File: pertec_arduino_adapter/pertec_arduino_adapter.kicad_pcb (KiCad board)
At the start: 2 copper layers, 88.9 x 53.3 mm, 15 parts, among them J1 Pertec J1, J10 SPI flash connector, J2 Pertec J2, J3 Mates with POWER, J4 Mates with ANALOG IN A0-A7, J5 Mates with ANALOG IN A8-A15, J6 Mates with JP6 ANALOG IN A8-A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, J7 Mates with PWM 0-7, J8 Mates with COMMUNICATION 14-21, J9 Mates with XIO DIGITAL 22-53

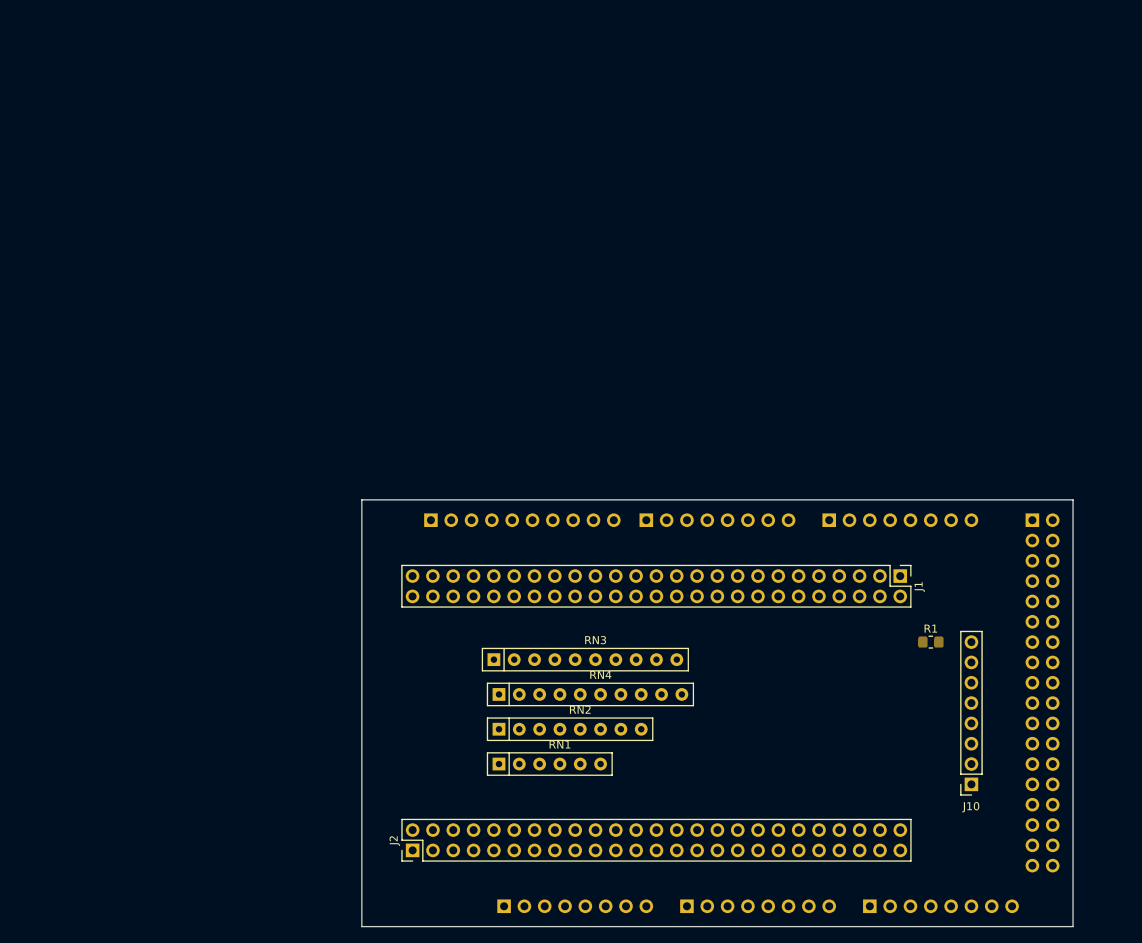
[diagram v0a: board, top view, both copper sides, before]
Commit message: Development checkpoint: started work on design for Adafruit Metro M4 Grand Central.  I'm aborting that development path and switching to the Teensy 4.1 because it's far faster and actually available.
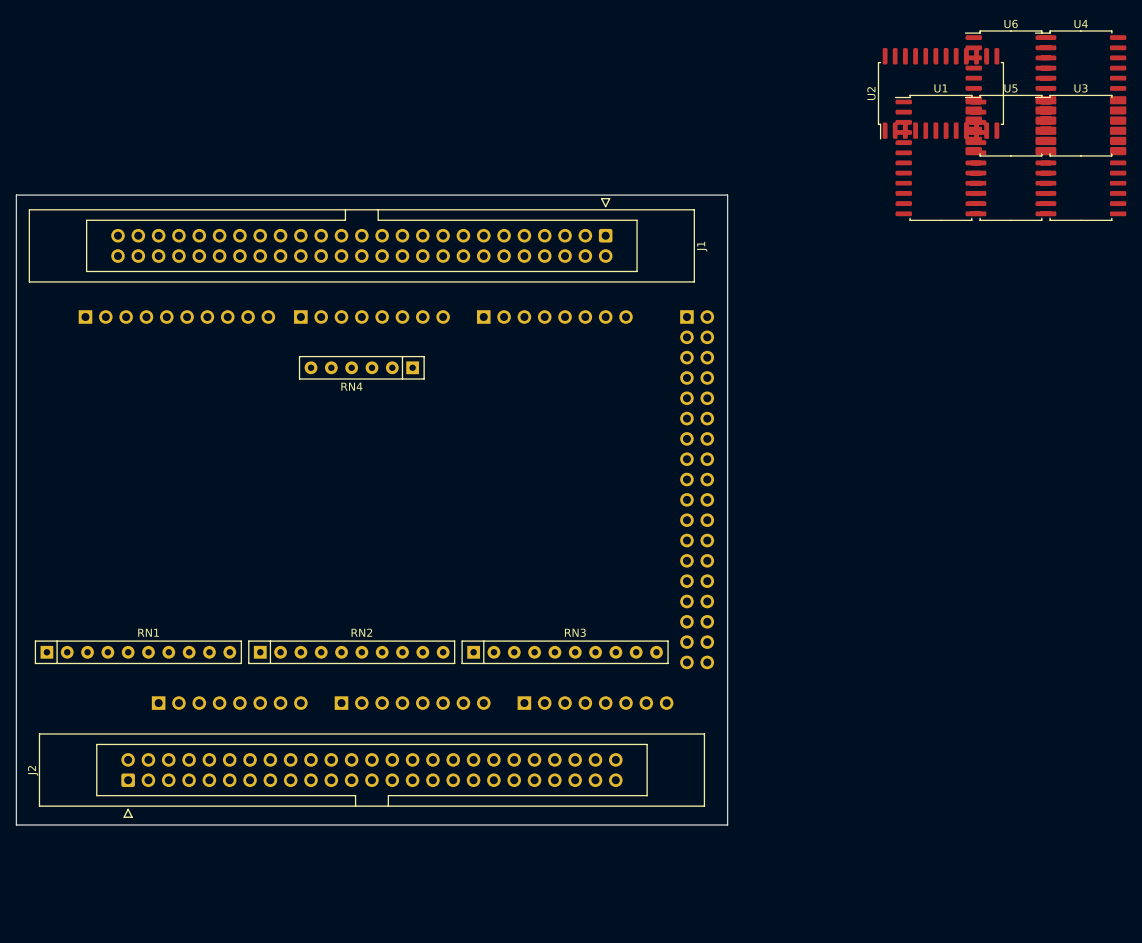
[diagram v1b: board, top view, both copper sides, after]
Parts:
- removed J10: SPI flash connector, Connector_PinSocket_2.54mm:PinSocket_1x08_P2.54mm_Vertical
- removed R1: 10 kΩ, Resistor_SMD:R_0805_2012Metric_Pad1.20x1.40mm_HandSolder
- added U1: SN74AVC8T245PW, pertec_arduino_adapter:SOIC-24W_7.5x15.4mm_P1.27mm, F.Cu at (191.8, 30.9)
- added U2: SN74AVC8T245PW, pertec_arduino_adapter:SOIC-24W_7.5x15.4mm_P1.27mm, F.Cu at (191.8, 22.9)
- added U3: SN74AVC8T245PW, pertec_arduino_adapter:SOIC-24W_7.5x15.4mm_P1.27mm, F.Cu at (209.3, 30.9)
- added U4: SN74AVC8T245PW, pertec_arduino_adapter:SOIC-24W_7.5x15.4mm_P1.27mm, F.Cu at (209.3, 22.9)
- added U5: SN74AVC8T245PW, pertec_arduino_adapter:SOIC-24W_7.5x15.4mm_P1.27mm, F.Cu at (200.5, 30.9)
- added U6: SN74AVC8T245PW, pertec_arduino_adapter:SOIC-24W_7.5x15.4mm_P1.27mm, F.Cu at (200.5, 22.9)
- J1: value Pertec J1 -> Conn_02x25_Odd_Even; footprint Connector_PinHeader_2.54mm:PinHeader_2x25_P2.54mm_Vertical -> pertec_arduino_adapter:IDC-Header_2x25_P2.54mm_Latch_Vertical
- J2: value Pertec J2 -> Conn_02x25_Odd_Even; footprint Connector_PinHeader_2.54mm:PinHeader_2x25_P2.54mm_Vertical -> pertec_arduino_adapter:IDC-Header_2x25_P2.54mm_Latch_Vertical
- J3: value Mates with POWER -> POWER; footprint Connector_PinHeader_2.54mm:PinHeader_1x08_P2.54mm_Vertical -> pertec_arduino_adapter:PinHeader_1x08_P2.54mm_Vertical
- J4: value Mates with ANALOG IN A0-A7 -> ANALOGL; footprint Connector_PinHeader_2.54mm:PinHeader_1x08_P2.54mm_Vertical -> pertec_arduino_adapter:PinHeader_1x08_P2.54mm_Vertical
- J5: value Mates with ANALOG IN A8-A15 -> ANALOGH; footprint Connector_PinHeader_2.54mm:PinHeader_1x08_P2.54mm_Vertical -> pertec_arduino_adapter:PinHeader_1x08_P2.54mm_Vertical
- J6: value Mates with JP6 ANALOG IN A8-A13+others -> Conn_02x18_Odd_Even; footprint Connector_PinHeader_2.54mm:PinHeader_1x10_P2.54mm_Vertical -> pertec_arduino_adapter:PinHeader_2x18_P2.54mm_Vertical_Mirror
- J7: value Mates with PWM 0-7 -> IOH; footprint Connector_PinHeader_2.54mm:PinHeader_1x08_P2.54mm_Vertical -> pertec_arduino_adapter:PinHeader_1x10_P2.54mm_Vertical
- J8: value Mates with COMMUNICATION 14-21 -> IOL; footprint Connector_PinHeader_2.54mm:PinHeader_1x08_P2.54mm_Vertical -> pertec_arduino_adapter:PinHeader_1x08_P2.54mm_Vertical
- J9: value Mates with XIO DIGITAL 22-53 -> UART; footprint pertec_arduino_adapter:PinHeader_2x18_P2.54mm_Vertical_Mirror -> pertec_arduino_adapter:PinHeader_1x08_P2.54mm_Vertical
- RN1: value R_Divider_Network04_Split -> R1=220Ω, R2=330Ω; footprint Resistor_THT:R_Array_SIP6 -> pertec_arduino_adapter:R_Array_SIP10
- RN2: value R_Divider_Network06_Split -> R1=220Ω, R2=330Ω; footprint Resistor_THT:R_Array_SIP8 -> pertec_arduino_adapter:R_Array_SIP10
- RN3: value R_Divider_Network08_Split -> R1=220Ω, R2=330Ω; footprint Resistor_THT:R_Array_SIP10 -> pertec_arduino_adapter:R_Array_SIP10
- RN4: value R_Divider_Network08_Split -> R1=220Ω, R2=330Ω; footprint Resistor_THT:R_Array_SIP10 -> pertec_arduino_adapter:R_Array_SIP6
- moved J7 74.6 mm to (84.8, 50.8)
- moved J9 73.1 mm to (134.6, 50.8), turned to -90 degrees
- moved J8 70.8 mm to (111.8, 50.8)
- moved RN1 58.2 mm to (80.0, 92.7)
- moved J1 56.3 mm to (149.9, 40.6)
- moved J4 50.1 mm to (116.8, 99.1)
- moved J5 50.1 mm to (139.7, 99.1)
- moved J3 50.1 mm to (94.0, 99.1)
- moved RN4 42.2 mm to (125.7, 57.1), turned to 180 degrees
- moved J6 40.9 mm to (160.0, 50.8), turned to 180 degrees
- moved J2 36.6 mm to (90.2, 108.7)
- moved RN2 31.4 mm to (106.7, 92.7)
- moved RN3 2.70 mm to (133.4, 92.7)
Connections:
- J1 pad 13: (no net) -> GNDREF
- J1 pad 15: (no net) -> GNDREF
- J1 pad 35: (no net) -> GNDREF
- J1 pad 43: (no net) -> GNDREF
- J2 pad 46: ITDA1 -> ITAD1
- J2 pad 49: (no net) -> GNDREF
- J2 pad 50: IDEN -> IHISP
- J3 pad 1: (no net) -> unconnected-(J3-Pad1)
- J3 pad 2: +5V -> +3V3
- J3 pad 3: (no net) -> ~{RESET}
- J3 pad 4: (no net) -> +3V3
- J3 pad 8: (no net) -> /VIN
- J4 pad 1: IR7 -> A0
- J4 pad 2: IR6 -> A1
- J4 pad 3: IR5 -> A2
- J4 pad 4: IR4 -> A3
- J4 pad 5: IR3 -> A4
- J4 pad 6: IR2 -> A5
- J4 pad 7: IR1 -> A6
- J4 pad 8: IR0 -> A7
- J5 pad 1: IFBY -> A8
- J5 pad 2: ILDP -> A9
- J5 pad 3: IEOT -> A10
- J5 pad 4: IRDY -> A11
- J5 pad 5: IRWD -> A12
- J5 pad 6: IFPT -> A13
- J5 pad 7: ISPEED -> A14
- J5 pad 8: IONL -> A15
- J6 pad 1: IHER -> +5V
- J6 pad 10: (no net) -> PCC_XCLK
- J6 pad 2: IFMK -> +5V
- J6 pad 3: (no net) -> D22
- J6 pad 4: GNDREF -> A10
- J6 pad 5: IRTH1 -> SCL_1
- J6 pad 6: IRTH2 -> SDA_1
- J6 pad 7: ILOL -> PCC_DEN1
- J6 pad 8: ISGL -> PCC_DEN2
- J6 pad 9: (no net) -> PCC_CLK
- J7 pad 1: (no net) -> SCL
- J7 pad 2: (no net) -> SDA
- J7 pad 3: (no net) -> AREF
- J7 pad 4: (no net) -> GND
- J7 pad 5: IRSTR -> D13
- J7 pad 6: IWSTR -> D12
- J7 pad 7: (no net) -> D11
- J7 pad 8: (no net) -> D10
- J8 pad 1: (no net) -> D7
- J8 pad 2: (no net) -> D6
- J8 pad 3: (no net) -> D5
- J8 pad 4: (no net) -> D4
- J8 pad 5: IDBY -> D3
- J8 pad 6: ICER -> D2
- J8 pad 7: IFMK -> D1
- J8 pad 8: IHER -> D0
- J9 pad 1: +5V -> UART3_TX
- J9 pad 2: +5V -> UART3_RX
- J9 pad 3: IW7 -> UART2_TX
- J9 pad 4: IW6 -> UART2_RX
- J9 pad 5: IW5 -> UART1_TX
- J9 pad 6: IW4 -> UART1_RX
- J9 pad 7: IW3 -> SDA
- J9 pad 8: IW2 -> SCL
- RN1 pad 2: IR3 -> IRP
- RN1 pad 3: ISPEED -> IR0
- RN1 pad 4: ICER -> IR1
- RN1 pad 5: IONL -> ILDP
- RN1 pad 6: +5V -> IR4
- RN2 pad 2: IRWD -> IFMK
- RN2 pad 3: IRP -> IDENT
- RN2 pad 4: IRSTR -> IR5
- RN2 pad 5: IWSTR -> IEOT
- RN2 pad 6: IDBY -> INRZ
- RN2 pad 7: IR2 -> IRDY
- RN2 pad 8: +5V -> IRWD
- RN3 pad 2: ILDP -> IRSTR
- RN3 pad 3: IHER -> IWSTR
- RN3 pad 4: INRZ -> IDBY
- RN3 pad 5: IFMK -> ISPEED
- RN3 pad 6: IR0 -> ICER
- RN3 pad 7: IR6 -> IONL
- RN3 pad 8: IFPT -> unconnected-(RN3-Pad8)
- RN3 pad 9: IR7 -> unconnected-(RN3-Pad9)
- RN4 pad 2: IR4 -> IFBY
- RN4 pad 3: IRDY -> IR2
- RN4 pad 4: IDENT -> IR3
- RN4 pad 5: IR1 -> unconnected-(RN4-Pad5)
- RN4 pad 6: IR5 -> +5V
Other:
- board size 88.9 x 53.3 mm -> 88.9 x 78.7 mm
- net class Default removed

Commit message: Development checkpoint: schematic complete, passes ERC, started layout.
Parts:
- removed J9: UART, pertec_arduino_adapter:PinHeader_1x08_P2.54mm_Vertical
- added BT1: CR2032, pertec_arduino_adapter:BatteryHolder_Keystone_1058_1x2032, F.Cu at (158.8, 74.9)
- added C1: 0.1 μF, pertec_arduino_adapter:C_Rect_L4.0mm_W2.5mm_P2.50mm, F.Cu at (114.3, 80.0)
- added C10: 0.1 μF, pertec_arduino_adapter:C_0805_2012Metric_Pad1.18x1.45mm_HandSolder, B.Cu at (97.8, 114.3)
- added C11: 0.1 μF, pertec_arduino_adapter:C_0805_2012Metric_Pad1.18x1.45mm_HandSolder, B.Cu at (157.7, 96.5)
- added C12: 0.1 μF, pertec_arduino_adapter:C_0805_2012Metric_Pad1.18x1.45mm_HandSolder, B.Cu at (171.4, 81.3)
- added C13: 0.1 μF, pertec_arduino_adapter:C_0805_2012Metric_Pad1.18x1.45mm_HandSolder, B.Cu at (172.7, 92.7)
- added C14: 0.1 μF, pertec_arduino_adapter:C_0805_2012Metric_Pad1.18x1.45mm_HandSolder, B.Cu at (166.4, 64.8)
- added C2: 0.1 μF, pertec_arduino_adapter:C_0805_2012Metric_Pad1.18x1.45mm_HandSolder, B.Cu at (110.5, 80.0)
- added C3: 0.1 μF, pertec_arduino_adapter:C_0805_2012Metric_Pad1.18x1.45mm_HandSolder, B.Cu at (97.8, 106.7)
- added C4: 0.1 μF, pertec_arduino_adapter:C_0805_2012Metric_Pad1.18x1.45mm_HandSolder, B.Cu at (146.1, 63.5)
- added C5: 0.1 μF, pertec_arduino_adapter:C_0805_2012Metric_Pad1.18x1.45mm_HandSolder, B.Cu at (146.3, 78.7)
- added C6: 0.1 μF, pertec_arduino_adapter:C_0805_2012Metric_Pad1.18x1.45mm_HandSolder, B.Cu at (152.4, 108.0)
- added C7: 0.1 μF, pertec_arduino_adapter:C_0805_2012Metric_Pad1.18x1.45mm_HandSolder, B.Cu at (120.7, 106.7)
- added C8: 0.1 μF, pertec_arduino_adapter:C_0805_2012Metric_Pad1.18x1.45mm_HandSolder, B.Cu at (120.7, 114.3)
- added C9: 0.1 μF, pertec_arduino_adapter:C_0805_2012Metric_Pad1.18x1.45mm_HandSolder, B.Cu at (166.4, 80.0)
- added Q1: BSS138, pertec_arduino_adapter:SOT-23, B.Cu at (113.0, 92.7)
- added Q2: BSS138, pertec_arduino_adapter:SOT-23, B.Cu at (119.4, 92.7)
- added R1: 10 kΩ, pertec_arduino_adapter:R_0805_2012Metric_Pad1.20x1.40mm_HandSolder, B.Cu at (113.0, 97.8)
- added R10: 10 kΩ, pertec_arduino_adapter:R_0805_2012Metric_Pad1.20x1.40mm_HandSolder, B.Cu at (120.7, 110.5)
- added R11: 10 kΩ, pertec_arduino_adapter:R_0805_2012Metric_Pad1.20x1.40mm_HandSolder, B.Cu at (169.2, 95.2)
- added R2: 10 kΩ, pertec_arduino_adapter:R_0805_2012Metric_Pad1.20x1.40mm_HandSolder, B.Cu at (119.4, 97.8)
- added R3: 10 kΩ, pertec_arduino_adapter:R_0805_2012Metric_Pad1.20x1.40mm_HandSolder, B.Cu at (108.0, 91.4)
- added R4: 10 kΩ, pertec_arduino_adapter:R_0805_2012Metric_Pad1.20x1.40mm_HandSolder, B.Cu at (125.7, 91.4)
- added R5: 10 kΩ, pertec_arduino_adapter:R_0805_2012Metric_Pad1.20x1.40mm_HandSolder, B.Cu at (119.4, 63.5)
- added R6: 10 kΩ, pertec_arduino_adapter:R_0805_2012Metric_Pad1.20x1.40mm_HandSolder, B.Cu at (114.3, 63.5)
- added R7: 10 kΩ, pertec_arduino_adapter:R_0805_2012Metric_Pad1.20x1.40mm_HandSolder, B.Cu at (109.2, 63.5)
- added R8: 10 kΩ, pertec_arduino_adapter:R_0805_2012Metric_Pad1.20x1.40mm_HandSolder, B.Cu at (119.4, 81.0)
- added R9: 10 kΩ, pertec_arduino_adapter:R_0805_2012Metric_Pad1.20x1.40mm_HandSolder, B.Cu at (97.8, 110.5)
- added U7: PCA9535DBR, pertec_arduino_adapter:SOIC-24W_7.5x15.4mm_P1.27mm, B.Cu at (118.1, 71.1)
- J3: value POWER -> Conn_02x03_Odd_Even; footprint pertec_arduino_adapter:PinHeader_1x08_P2.54mm_Vertical -> pertec_arduino_adapter:PinSocket_2x03_P2.00mm_Vertical_Mirror; moved to F.Cu
- J4: value ANALOGL -> Conn_01x24; footprint pertec_arduino_adapter:PinHeader_1x08_P2.54mm_Vertical -> pertec_arduino_adapter:PinSocket_1x24_P2.54mm_Vertical; moved to F.Cu
- J5: value ANALOGH -> Conn_01x24; footprint pertec_arduino_adapter:PinHeader_1x08_P2.54mm_Vertical -> pertec_arduino_adapter:PinSocket_1x24_P2.54mm_Vertical; moved to F.Cu
- J6: value Conn_02x18_Odd_Even -> Conn_01x05; footprint pertec_arduino_adapter:PinHeader_2x18_P2.54mm_Vertical_Mirror -> pertec_arduino_adapter:PinSocket_1x05_P2.54mm_Vertical; moved to F.Cu
- J7: value IOH -> RJ45_Cetus_J1B1211CCD; footprint pertec_arduino_adapter:PinHeader_1x10_P2.54mm_Vertical -> pertec_arduino_adapter:RJ45_Cetus_J1B1211CCD_Horizontal; moved to F.Cu
- J8: value IOL -> Conn_02x03_Odd_Even; footprint pertec_arduino_adapter:PinHeader_1x08_P2.54mm_Vertical -> pertec_arduino_adapter:PinHeader_2x03_P2.54mm_Vertical; moved to F.Cu
- U1, U2, U3, U4, U5, U6: value SN74AVC8T245PW -> SN74LVC8T245NSR; footprint pertec_arduino_adapter:SOIC-24W_7.5x15.4mm_P1.27mm -> pertec_arduino_adapter:SO-24_5.3x15mm_P1.27mm; moved to B.Cu
- moved U2 120.4 mm to (109.2, 110.5), turned to -90 degrees
- moved U4 116.8 mm to (132.1, 110.5), turned to -90 degrees
- moved RN1 96.0 mm to (170.2, 59.7), turned to 180 degrees
- moved J1 94.3 mm to (100.3, 120.9), turned to 90 degrees
- moved J2 93.2 mm to (162.6, 50.0), turned to -90 degrees
- moved U5 81.9 mm to (163.8, 104.1), turned to -90 degrees
- moved U3 80.4 mm to (139.7, 71.1), turned to 90 degrees
- moved U6 75.1 mm to (162.6, 87.6), turned to 90 degrees
- moved RN4 60.8 mm to (152.4, 111.8), turned to 0 degrees
- moved U1 53.3 mm to (160.0, 73.7), turned to 90 degrees
- moved J5 52.2 mm to (87.6, 102.8), turned to 90 degrees
- moved RN2 49.5 mm to (143.5, 59.7), turned to 180 degrees
- moved J6 47.6 mm to (133.4, 90.2), turned to 0 degrees
- moved RN3 36.9 mm to (116.8, 59.7), turned to 180 degrees
- moved J8 34.9 mm to (130.8, 80.0)
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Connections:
- J2 pad 50: IHISP -> IDEN
- J3 pad 1: unconnected-(J3-Pad1) -> ETHERNET_TM
- J3 pad 2: +3V3 -> ETHERNET_TP
- J3 pad 3: ~{RESET} -> ETHERNET_LED
- J3 pad 4: +3V3 -> ETHERNET_G
- J3 pad 5: +5V -> ETHERNET_RP
- J3 pad 6: GNDREF -> ETHERNET_RM
- J4 pad 1: A0 -> +5V
- J4 pad 2: A1 -> GNDREF
- J4 pad 3: A2 -> +3V3
- J4 pad 4: A3 -> GPIO_AD_B1_09
- J4 pad 5: A4 -> GPIO_AD_B1_08
- J4 pad 6: A5 -> GPIO_AD_B1_11
- J4 pad 7: A6 -> GPIO_AD_B1_10
- J4 pad 8: A7 -> GPIO_AD_B1_00
- J5 pad 1: A8 -> GNDREF
- J5 pad 2: A9 -> GPIO_AD_B0_03
- J5 pad 3: A10 -> GPIO_AD_B0_02
- J5 pad 4: A11 -> GPIO_EMC_04
- J5 pad 5: A12 -> GPIO_EMC_05
- J5 pad 6: A13 -> GPIO_EMC_06
- J5 pad 7: A14 -> GPIO_EMC_08
- J5 pad 8: A15 -> GPIO_B0_10
- J6 pad 1: +5V -> unconnected-(J6-Pad1)
- J6 pad 2: +5V -> unconnected-(J6-Pad2)
- J6 pad 3: D22 -> GNDREF
- J6 pad 4: A10 -> unconnected-(J6-Pad4)
- J6 pad 5: SCL_1 -> Net-(BT1-Pad1)
- J7 pad 1: SCL -> ETHERNET_TP
- J7 pad 10: D8 -> ETHERNET_LED
- J7 pad 2: SDA -> Net-(J7-Pad2)
- J7 pad 3: AREF -> ETHERNET_TM
- J7 pad 4: GND -> ETHERNET_RP
- J7 pad 5: D13 -> Net-(J7-Pad2)
- J7 pad 6: D12 -> ETHERNET_RM
- J7 pad 7: D11 -> unconnected-(J7-Pad7)
- J7 pad 8: D10 -> ETHERNET_G
- J7 pad 9: D9 -> ETHERNET_G
- J8 pad 1: D7 -> GNDREF
- J8 pad 2: D6 -> SPARE0
- J8 pad 3: D5 -> GNDREF
- J8 pad 4: D4 -> SPARE1
- J8 pad 5: D3 -> GNDREF
- J8 pad 6: D2 -> GPIO_EMC_31
- U1 pad 1: unconnected-(U1-Pad1) -> +3V3
- U1 pad 10: unconnected-(U1-Pad10) -> GPIO_B1_12
- U1 pad 11: Net-(U1-Pad11) -> GNDREF
- U1 pad 12: Net-(U1-Pad11) -> GNDREF
- U1 pad 13: Net-(U1-Pad11) -> GNDREF
- U1 pad 14: unconnected-(U1-Pad14) -> IHER
- U1 pad 15: unconnected-(U1-Pad15) -> IR6
- U1 pad 16: unconnected-(U1-Pad16) -> IR7
- U1 pad 17: unconnected-(U1-Pad17) -> IR4
- U1 pad 18: unconnected-(U1-Pad18) -> ILDP
- U1 pad 19: unconnected-(U1-Pad19) -> IR1
- U1 pad 2: unconnected-(U1-Pad2) -> GNDREF
- U1 pad 20: unconnected-(U1-Pad20) -> IR0
- U1 pad 21: unconnected-(U1-Pad21) -> IRP
- U1 pad 22: unconnected-(U1-Pad22) -> GNDREF
- U1 pad 23: unconnected-(U1-Pad23) -> +5V
- U1 pad 24: unconnected-(U1-Pad24) -> +5V
- U1 pad 3: unconnected-(U1-Pad3) -> GPIO_AD_B0_02
- U1 pad 4: unconnected-(U1-Pad4) -> GPIO_AD_B1_07
- U1 pad 5: unconnected-(U1-Pad5) -> GPIO_AD_B1_06
- U1 pad 6: unconnected-(U1-Pad6) -> GPIO_EMC_32
- U1 pad 7: unconnected-(U1-Pad7) -> GPIO_AD_B1_03
- U1 pad 8: unconnected-(U1-Pad8) -> GPIO_AD_B1_00
- U1 pad 9: unconnected-(U1-Pad9) -> GPIO_AD_B1_01
- U2 pad 1: unconnected-(U2-Pad1) -> +3V3
- U2 pad 10: unconnected-(U2-Pad10) -> GPIO_B1_01
- U2 pad 11: Net-(U2-Pad11) -> GNDREF
- U2 pad 12: Net-(U2-Pad11) -> GNDREF
- U2 pad 13: Net-(U2-Pad11) -> GNDREF
- U2 pad 14: unconnected-(U2-Pad14) -> IWP
- U2 pad 15: unconnected-(U2-Pad15) -> IREW
- U2 pad 16: unconnected-(U2-Pad16) -> IREV
- U2 pad 17: unconnected-(U2-Pad17) -> IW1
- U2 pad 18: unconnected-(U2-Pad18) -> IW0
- U2 pad 19: unconnected-(U2-Pad19) -> IGO
- U2 pad 2: unconnected-(U2-Pad2) -> Net-(U2-Pad2)
- U2 pad 20: unconnected-(U2-Pad20) -> IW4
- U2 pad 21: unconnected-(U2-Pad21) -> ILWD
- U2 pad 22: unconnected-(U2-Pad22) -> GNDREF
- U2 pad 23: unconnected-(U2-Pad23) -> +5V
- U2 pad 24: unconnected-(U2-Pad24) -> +5V
- U2 pad 3: unconnected-(U2-Pad3) -> GPIO_B0_03
- U2 pad 4: unconnected-(U2-Pad4) -> GPIO_AD_B1_11
- U2 pad 5: unconnected-(U2-Pad5) -> GPIO_B0_10
- U2 pad 6: unconnected-(U2-Pad6) -> GPIO_AD_B1_15
- U2 pad 7: unconnected-(U2-Pad7) -> GPIO_AD_B1_14
- U2 pad 8: unconnected-(U2-Pad8) -> GPIO_B0_11
- U2 pad 9: unconnected-(U2-Pad9) -> GPIO_B1_00
- U3 pad 1: unconnected-(U3-Pad1) -> +3V3
- U3 pad 10: unconnected-(U3-Pad10) -> GPIO_EMC_06
- U3 pad 11: Net-(U3-Pad11) -> GNDREF
- U3 pad 12: Net-(U3-Pad11) -> GNDREF
- U3 pad 13: Net-(U3-Pad11) -> GNDREF
- U3 pad 14: unconnected-(U3-Pad14) -> IDBY
- U3 pad 15: unconnected-(U3-Pad15) -> IWSTR
- U3 pad 16: unconnected-(U3-Pad16) -> IRSTR
- U3 pad 17: unconnected-(U3-Pad17) -> IFPT
- U3 pad 18: unconnected-(U3-Pad18) -> IRDY
- U3 pad 19: unconnected-(U3-Pad19) -> IEOT
- U3 pad 2: unconnected-(U3-Pad2) -> GNDREF
- U3 pad 20: unconnected-(U3-Pad20) -> IR5
- U3 pad 21: unconnected-(U3-Pad21) -> IFMK
- U3 pad 22: unconnected-(U3-Pad22) -> GNDREF
- U3 pad 23: unconnected-(U3-Pad23) -> +5V
- U3 pad 24: unconnected-(U3-Pad24) -> +5V
- U3 pad 3: unconnected-(U3-Pad3) -> GPIO_AD_B0_03
- U3 pad 4: unconnected-(U3-Pad4) -> GPIO_AD_B1_02
- U3 pad 5: unconnected-(U3-Pad5) -> GPIO_EMC_36
- U3 pad 6: unconnected-(U3-Pad6) -> GPIO_EMC_04
- U3 pad 7: unconnected-(U3-Pad7) -> GPIO_EMC_05
- U3 pad 8: unconnected-(U3-Pad8) -> GPIO_B1_02
- U3 pad 9: unconnected-(U3-Pad9) -> GPIO_B1_03
- U4 pad 1: unconnected-(U4-Pad1) -> +3V3
- U4 pad 10: unconnected-(U4-Pad10) -> GPIO_B0_01
- U4 pad 11: Net-(U4-Pad11) -> GNDREF
- U4 pad 12: Net-(U4-Pad11) -> GNDREF
- U4 pad 13: Net-(U4-Pad11) -> GNDREF
- U4 pad 14: unconnected-(U4-Pad14) -> IERASE
- U4 pad 15: unconnected-(U4-Pad15) -> IEDIT
- U4 pad 16: unconnected-(U4-Pad16) -> IWRT
- U4 pad 17: unconnected-(U4-Pad17) -> IW5
- U4 pad 18: unconnected-(U4-Pad18) -> IW2
- U4 pad 19: unconnected-(U4-Pad19) -> IW6
- U4 pad 2: unconnected-(U4-Pad2) -> Net-(U4-Pad2)
- U4 pad 20: unconnected-(U4-Pad20) -> IW3
- U4 pad 21: unconnected-(U4-Pad21) -> IW7
- U4 pad 22: unconnected-(U4-Pad22) -> GNDREF
- U4 pad 23: unconnected-(U4-Pad23) -> +5V
- U4 pad 24: unconnected-(U4-Pad24) -> +5V
- U4 pad 3: unconnected-(U4-Pad3) -> GPIO_AD_B1_08
- U4 pad 4: unconnected-(U4-Pad4) -> GPIO_AD_B1_12
- U4 pad 5: unconnected-(U4-Pad5) -> GPIO_AD_B1_09
- U4 pad 6: unconnected-(U4-Pad6) -> GPIO_AD_B1_13
- U4 pad 7: unconnected-(U4-Pad7) -> GPIO_AD_B1_10
- U4 pad 8: unconnected-(U4-Pad8) -> GPIO_B0_00
- U4 pad 9: unconnected-(U4-Pad9) -> GPIO_B0_02
- U5 pad 1: unconnected-(U5-Pad1) -> +3V3
- U5 pad 11: Net-(U5-Pad11) -> GNDREF
- U5 pad 12: Net-(U5-Pad11) -> GNDREF
- U5 pad 13: Net-(U5-Pad11) -> GNDREF
- U5 pad 18: unconnected-(U5-Pad18) -> IR3
- U5 pad 19: unconnected-(U5-Pad19) -> IR2
- U5 pad 2: unconnected-(U5-Pad2) -> GNDREF
- U5 pad 20: unconnected-(U5-Pad20) -> IFBY
- U5 pad 21: unconnected-(U5-Pad21) -> ICER
- U5 pad 22: unconnected-(U5-Pad22) -> GNDREF
- U5 pad 23: unconnected-(U5-Pad23) -> +5V
- U5 pad 24: unconnected-(U5-Pad24) -> +5V
- U5 pad 3: unconnected-(U5-Pad3) -> GPIO_B1_13
- U5 pad 4: unconnected-(U5-Pad4) -> GPIO_EMC_07
- U5 pad 5: unconnected-(U5-Pad5) -> GPIO_AD_B1_05
- U5 pad 6: unconnected-(U5-Pad6) -> GPIO_AD_B1_04
- U6 pad 1: unconnected-(U6-Pad1) -> +3V3
- U6 pad 10: unconnected-(U6-Pad10) -> GPIO_EMC_37
- U6 pad 11: Net-(U6-Pad11) -> GNDREF
- U6 pad 12: Net-(U6-Pad11) -> GNDREF
- U6 pad 13: Net-(U6-Pad11) -> GNDREF
- U6 pad 14: unconnected-(U6-Pad14) -> IOFL
- U6 pad 15: unconnected-(U6-Pad15) -> IWFM
- U6 pad 2: unconnected-(U6-Pad2) -> Net-(U6-Pad2)
- U6 pad 22: unconnected-(U6-Pad22) -> GNDREF
- U6 pad 23: unconnected-(U6-Pad23) -> +5V
- U6 pad 24: unconnected-(U6-Pad24) -> +5V
- U6 pad 9: unconnected-(U6-Pad9) -> GPIO_B0_12
